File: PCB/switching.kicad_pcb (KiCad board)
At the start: 2 copper layers, 108.8 x 37.9 mm, 32 parts, among them J1 CURRENT, J2 24VAC, J3 3V3, U1 BD9G101G

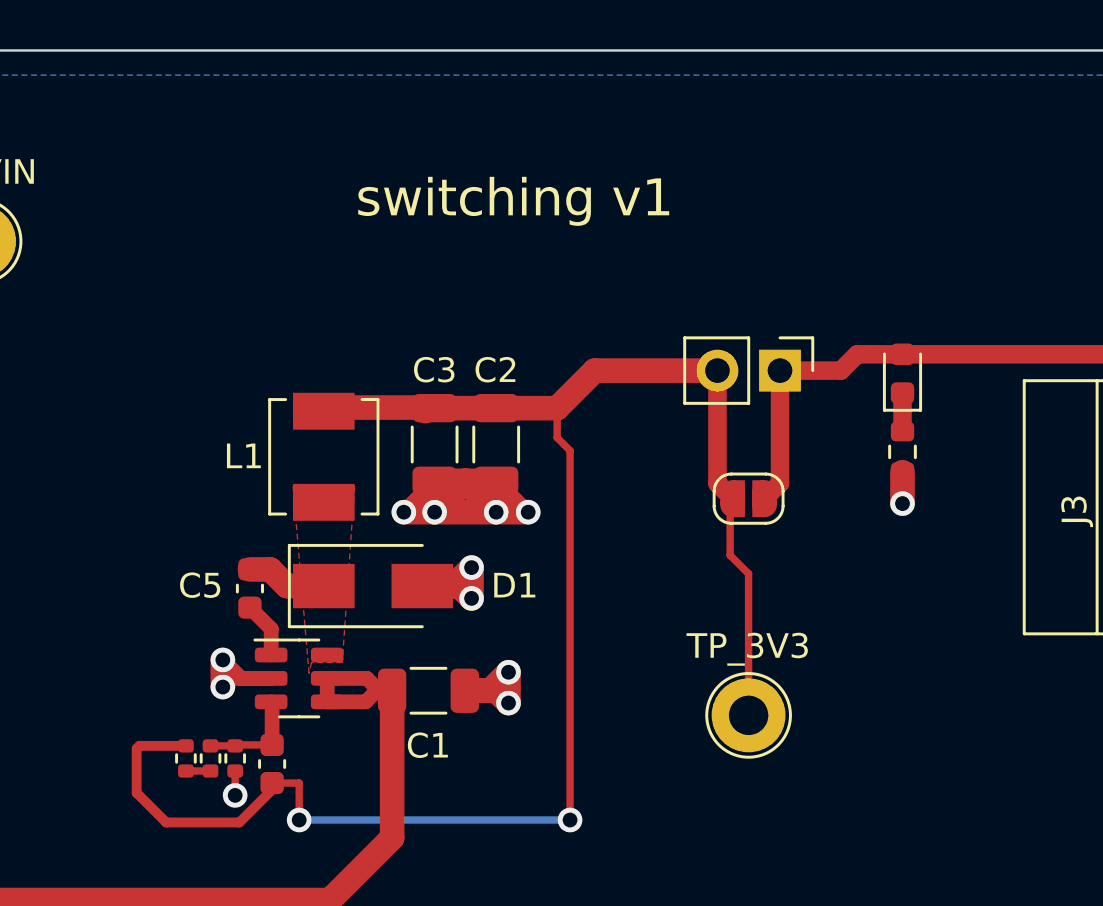
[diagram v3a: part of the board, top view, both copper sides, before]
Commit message: add ground testpoints
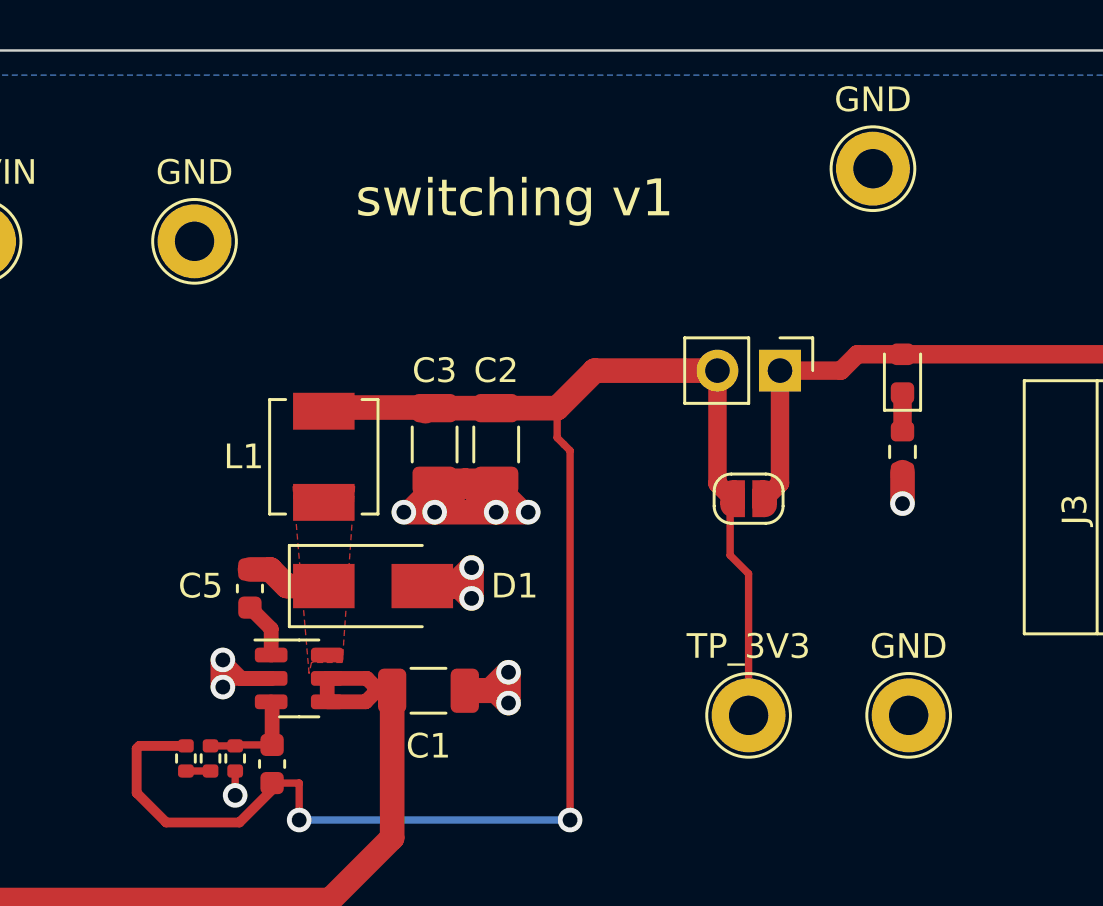
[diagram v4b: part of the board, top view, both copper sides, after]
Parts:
- added TP1: GND, TestPoint:TestPoint_Loop_D2.60mm_Drill1.6mm_Beaded, F.Cu at (92.2, 54.8)
- added TP5: GND, TestPoint:TestPoint_Loop_D2.60mm_Drill1.6mm_Beaded, F.Cu at (121.2, 74.0)
- added TP6: GND, TestPoint:TestPoint_Loop_D2.60mm_Drill1.6mm_Beaded, F.Cu at (119.8, 51.8)
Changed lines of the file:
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@@
   (net 12 "Net-(C1-Pad1)")
   (net 13 "Net-(D6-Pad2)")
+  (footprint "TestPoint:TestPoint_Loop_D2.60mm_Drill1.6mm_Beaded" (layer "F.Cu")
+    (at 119.8 51.8)
+    (descr "wire loop with bead as test point, loop diameter2.6mm, hole diameter 1.6mm")
+    (tags "test point wire loop bead")
+    (property "LCSC" "a")
+    (property "Sheetfile" "switching.kicad_sch")
+    (property "Sheetname" "")
+    (attr through_hole)
+    (fp_text reference "TP6" (at 0.7 2.5) (layer "F.SilkS") hide
+      (effects (font (size 1 1) (thickness 0.15)))
+    )
+    (fp_text value "GND" (at 0 -2.8) (layer "F.SilkS")
+      (effects (font (size 1 1) (thickness 0.15)))
+    )
+    (fp_text user "${REFERENCE}" (at 0.7 2.5) (layer "F.Fab")
+      (effects (font (size 1 1) (thickness 0.15)))
+    )
+    (fp_circle (center 0 0) (end 1.7 0) (layer "F.SilkS") (width 0.12) (fill none))
+    (fp_circle (center 0 0) (end 2 0) (layer "F.CrtYd") (width 0.05) (fill none))
+    (fp_line (start -1.3 0.3) (end 1.3 0.3) (layer "F.Fab") (width 0.12))
+    (fp_line (start 1.3 0.3) (end 1.3 -0.3) (layer "F.Fab") (width 0.12))
+    (fp_line (start -1.3 -0.3) (end -1.3 0.3) (layer "F.Fab") (width 0.12))
+    (fp_line (start 1.3 -0.3) (end -1.3 -0.3) (layer "F.Fab") (width 0.12))
+    (fp_circle (center 0 0) (end 1.5 0) (layer "F.Fab") (width 0.12) (fill none))
+    (pad "1" thru_hole circle (at 0 0) (size 3 3) (drill 1.6) (layers *.Cu *.Mask)
+      (net 1 "GND") (pinfunction "1") (pintype "passive"))
+    (model "${KICAD6_3DMODEL_DIR}/TestPoint.3dshapes/TestPoint_Loop_D2.60mm_Drill1.6mm_Beaded.wrl"
+      (offset (xyz 0 0 0))
+      (scale (xyz 1 1 1))
+      (rotate (xyz 0 0 0))
+    )
+  )
   (footprint "MountingHole:MountingHole_3.2mm_M3" (layer "F.Cu")
     (at 132.75 51)
@@
     (pad "1" thru_hole circle (at 0 0) (size 3 3) (drill 1.6) (layers *.Cu *.Mask)
       (net 3 "Net-(D2-Pad1)") (pinfunction "1") (pintype "passive"))
+    (model "${KICAD6_3DMODEL_DIR}/TestPoint.3dshapes/TestPoint_Loop_D2.60mm_Drill1.6mm_Beaded.wrl"
+      (offset (xyz 0 0 0))
+      (scale (xyz 1 1 1))
+      (rotate (xyz 0 0 0))
+    )
+  )
+  (footprint "TestPoint:TestPoint_Loop_D2.60mm_Drill1.6mm_Beaded" (layer "F.Cu")
+    (at 92.25 54.75)
+    (descr "wire loop with bead as test point, loop diameter2.6mm, hole diameter 1.6mm")
+    (tags "test point wire loop bead")
+    (property "LCSC" "a")
+    (property "Sheetfile" "switching.kicad_sch")
+    (property "Sheetname" "")
+    (attr through_hole)
+    (fp_text reference "TP1" (at 0.7 2.5) (layer "F.SilkS") hide
+      (effects (font (size 1 1) (thickness 0.15)))
+    )
+    (fp_text value "GND" (at 0 -2.8) (layer "F.SilkS")
+      (effects (font (size 1 1) (thickness 0.15)))
+    )
+    (fp_text user "${REFERENCE}" (at 0.7 2.5) (layer "F.Fab")
+      (effects (font (size 1 1) (thickness 0.15)))
+    )
+    (fp_circle (center 0 0) (end 1.7 0) (layer "F.SilkS") (width 0.12) (fill none))
+    (fp_circle (center 0 0) (end 2 0) (layer "F.CrtYd") (width 0.05) (fill none))
+    (fp_line (start 1.3 0.3) (end 1.3 -0.3) (layer "F.Fab") (width 0.12))
+    (fp_line (start -1.3 0.3) (end 1.3 0.3) (layer "F.Fab") (width 0.12))
+    (fp_line (start 1.3 -0.3) (end -1.3 -0.3) (layer "F.Fab") (width 0.12))
+    (fp_line (start -1.3 -0.3) (end -1.3 0.3) (layer "F.Fab") (width 0.12))
+    (fp_circle (center 0 0) (end 1.5 0) (layer "F.Fab") (width 0.12) (fill none))
+    (pad "1" thru_hole circle (at 0 0) (size 3 3) (drill 1.6) (layers *.Cu *.Mask)
+      (net 1 "GND") (pinfunction "1") (pintype "passive"))
     (model "${KICAD6_3DMODEL_DIR}/TestPoint.3dshapes/TestPoint_Loop_D2.60mm_Drill1.6mm_Beaded.wrl"
       (offset (xyz 0 0 0))
@@
       (offset (xyz 0 0 0))
       (scale (xyz 1 1 1))
+      (rotate (xyz 0 0 0))
+    )
+  )
+  (footprint "TestPoint:TestPoint_Loop_D2.60mm_Drill1.6mm_Beaded" (layer "F.Cu")
+    (at 121.25 74)
+    (descr "wire loop with bead as test point, loop diameter2.6mm, hole diameter 1.6mm")
+    (tags "test point wire loop bead")
+    (property "LCSC" "a")
+    (property "Sheetfile" "switching.kicad_sch")
+    (property "Sheetname" "")
+    (attr through_hole)
+    (fp_text reference "TP5" (at 0.7 2.5) (layer "F.SilkS") hide
+      (effects (font (size 1 1) (thickness 0.15)))
+    )
+    (fp_text value "GND" (at 0 -2.8) (layer "F.SilkS")
+      (effects (font (size 1 1) (thickness 0.15)))
+    )
+    (fp_text user "${REFERENCE}" (at 0.7 2.5) (layer "F.Fab")
+      (effects (font (size 1 1) (thickness 0.15)))
+    )
+    (fp_circle (center 0 0) (end 1.7 0) (layer "F.SilkS") (width 0.12) (fill none))
+    (fp_circle (center 0 0) (end 2 0) (layer "F.CrtYd") (width 0.05) (fill none))
+    (fp_line (start -1.3 -0.3) (end -1.3 0.3) (layer "F.Fab") (width 0.12))
+    (fp_line (start -1.3 0.3) (end 1.3 0.3) (layer "F.Fab") (width 0.12))
+    (fp_line (start 1.3 -0.3) (end -1.3 -0.3) (layer "F.Fab") (width 0.12))
+    (fp_line (start 1.3 0.3) (end 1.3 -0.3) (layer "F.Fab") (width 0.12))
+    (fp_circle (center 0 0) (end 1.5 0) (layer "F.Fab") (width 0.12) (fill none))
+    (pad "1" thru_hole circle (at 0 0) (size 3 3) (drill 1.6) (layers *.Cu *.Mask)
+      (net 1 "GND") (pinfunction "1") (pintype "passive"))
+    (model "${KICAD6_3DMODEL_DIR}/TestPoint.3dshapes/TestPoint_Loop_D2.60mm_Drill1.6mm_Beaded.wrl"
+      (offset (xyz 0 0 0))
+      (scale (xyz 1 1 1))

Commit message: JLCJLCJLCJLC
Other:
- board text added: "JLCJLCJLCJLC"
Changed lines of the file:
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@@
   )
   (gr_rect (start 27.4 47) (end 136.2 84.9) (layer "Edge.Cuts") (width 0.1) (fill none))
+  (gr_text "JLCJLCJLCJLC" (at 80.8 83) (layer "B.SilkS")
+    (effects (font (size 1.5 1.5) (thickness 0.3)) (justify mirror))
+  )
   (gr_text "switching v1" (at 105.25 53) (layer "F.SilkS")
     (effects (font (size 1.5 1.5) (thickness 0.3)))

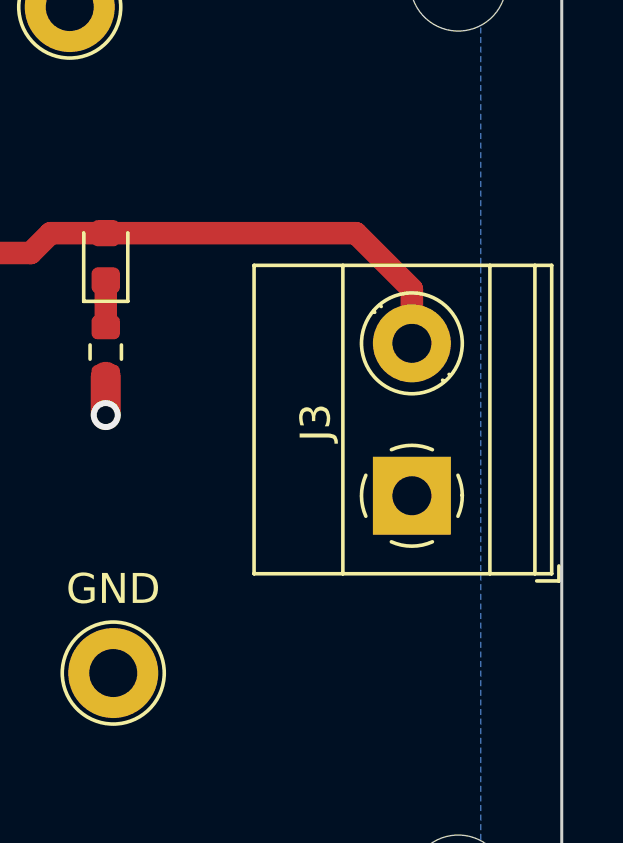
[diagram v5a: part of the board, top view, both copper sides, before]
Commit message: silkscreen update for polarity
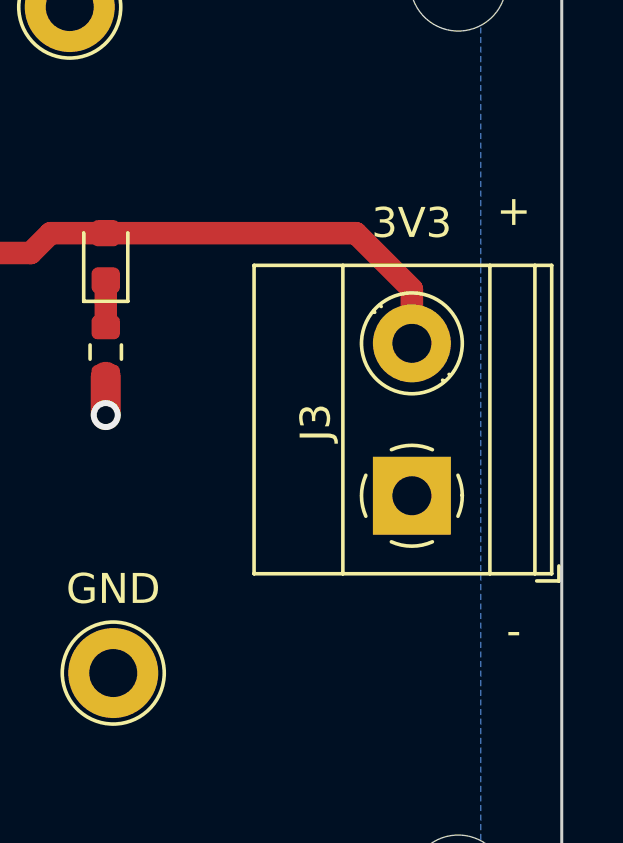
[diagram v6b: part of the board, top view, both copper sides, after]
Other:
- board text added: "+"
- board text added: "-"
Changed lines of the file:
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@@
       (effects (font (size 1 1) (thickness 0.15)))
     )
-    (fp_text value "3V3" (at 2.54 5.66 90) (layer "F.Fab")
+    (fp_text value "3V3" (at 9.09 -0.005 180) (layer "F.SilkS")
       (effects (font (size 1 1) (thickness 0.15)))
     )
@@
     (effects (font (size 1.5 1.5) (thickness 0.3)) (justify mirror))
   )
+  (gr_text "-" (at 134.6 72.6) (layer "F.SilkS")
+    (effects (font (size 1 1) (thickness 0.15)))
+  )
   (gr_text "switching v1" (at 105.25 53) (layer "F.SilkS")
     (effects (font (size 1.5 1.5) (thickness 0.3)))
   )
+  (gr_text "+" (at 134.6 58.6) (layer "F.SilkS")
+    (effects (font (size 1 1) (thickness 0.15)))
+  )
   (segment (start 103 68.75) (end 103.5 69.25) (width 1) (layer "F.Cu") (net 1))

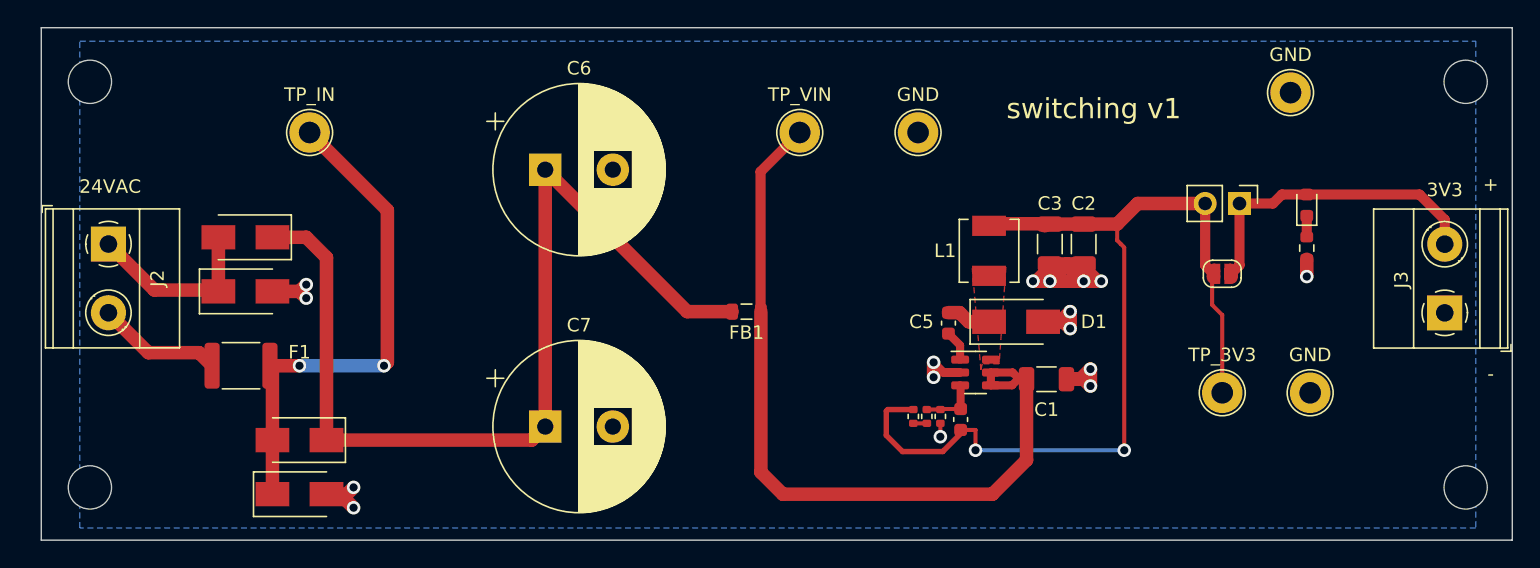
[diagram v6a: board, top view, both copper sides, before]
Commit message: smaller and smd only to use in designs
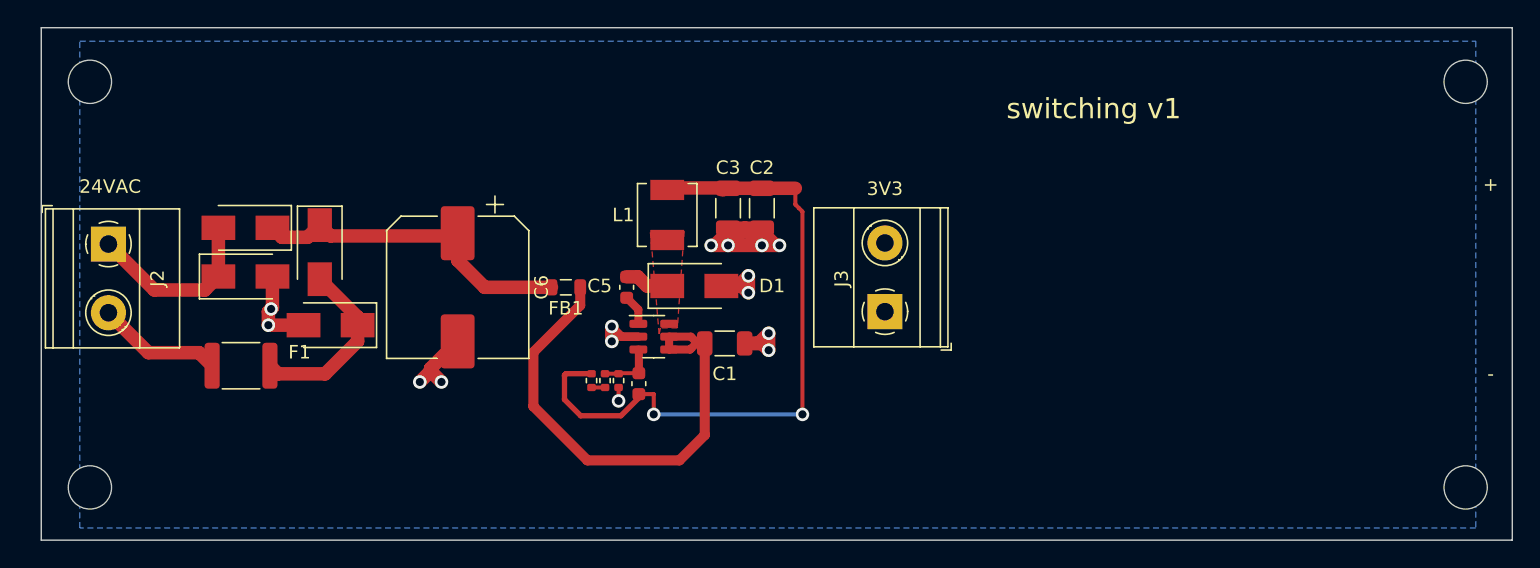
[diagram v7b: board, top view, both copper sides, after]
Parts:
- removed C7: 470uF 50V, Capacitor_THT:CP_Radial_D12.5mm_P5.00mm
- removed D6: 3V3POWER, LED_SMD:LED_0603_1608Metric
- removed J1: CURRENT, Connector_PinHeader_2.54mm:PinHeader_1x02_P2.54mm_Vertical
- removed JP1: CURRENTJUMP, Jumper:SolderJumper-2_P1.3mm_Open_RoundedPad1.0x1.5mm
- removed R1: 1k, Resistor_SMD:R_0603_1608Metric
- removed TP1, TP5, TP6: GND, TestPoint:TestPoint_Loop_D2.60mm_Drill1.6mm_Beaded
- removed TP2: TP_IN, TestPoint:TestPoint_Loop_D2.60mm_Drill1.6mm_Beaded
- removed TP3: TP_VIN, TestPoint:TestPoint_Loop_D2.60mm_Drill1.6mm_Beaded
- removed TP4: TP_3V3, TestPoint:TestPoint_Loop_D2.60mm_Drill1.6mm_Beaded
- C6: footprint Capacitor_THT:CP_Radial_D12.5mm_P5.00mm -> Capacitor_SMD:CP_Elec_10x10
- moved J3 41.4 mm to (89.8, 68.0)
- moved R11 23.9 mm to (68.1, 73.1)
- moved R12 23.9 mm to (69.1, 73.1)
- moved R2 23.9 mm to (70.1, 73.1)
- moved C4 23.9 mm to (71.6, 73.3)
- moved C1 23.9 mm to (78.0, 70.3)
- moved C2 23.9 mm to (80.7, 60.4)
- moved C3 23.9 mm to (78.2, 60.4)
- moved C5 23.9 mm to (70.7, 66.2)
- moved D1 23.9 mm to (75.7, 66.1)
- moved L1 23.9 mm to (73.7, 60.9)
- moved U1 23.9 mm to (72.7, 69.8)
- moved D3 14.0 mm to (48.0, 63.6), turned to -90 degrees
- moved FB1 13.5 mm to (66.2, 66.2)
- moved D2 12.7 mm to (48.8, 69.0), turned to 180 degrees
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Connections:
- net /BST renamed Net-(C5-Pad1)
- J3 pad 2: Net-(D6-Pad2) -> +3.3V
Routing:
- net Net-(C6-Pad1): track 71.9 -> 24.5 mm
- net Net-(D2-Pad1): track 37.7 -> 13.5 mm, vias 2 -> 0
- net Net-(D6-Pad2): track 23.5 -> 0.00 mm
- net +3.3V: track 72.2 -> 50.4 mm
- net Net-(C1-Pad1): track 59.1 -> 37.6 mm
- net GND: track 44.1 -> 46.8 mm, vias 16 -> 15
- net Net-(D6-Pad1): track 1.56 -> 0.00 mm
